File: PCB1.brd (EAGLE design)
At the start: 101.3 x 61 mm, 38 parts

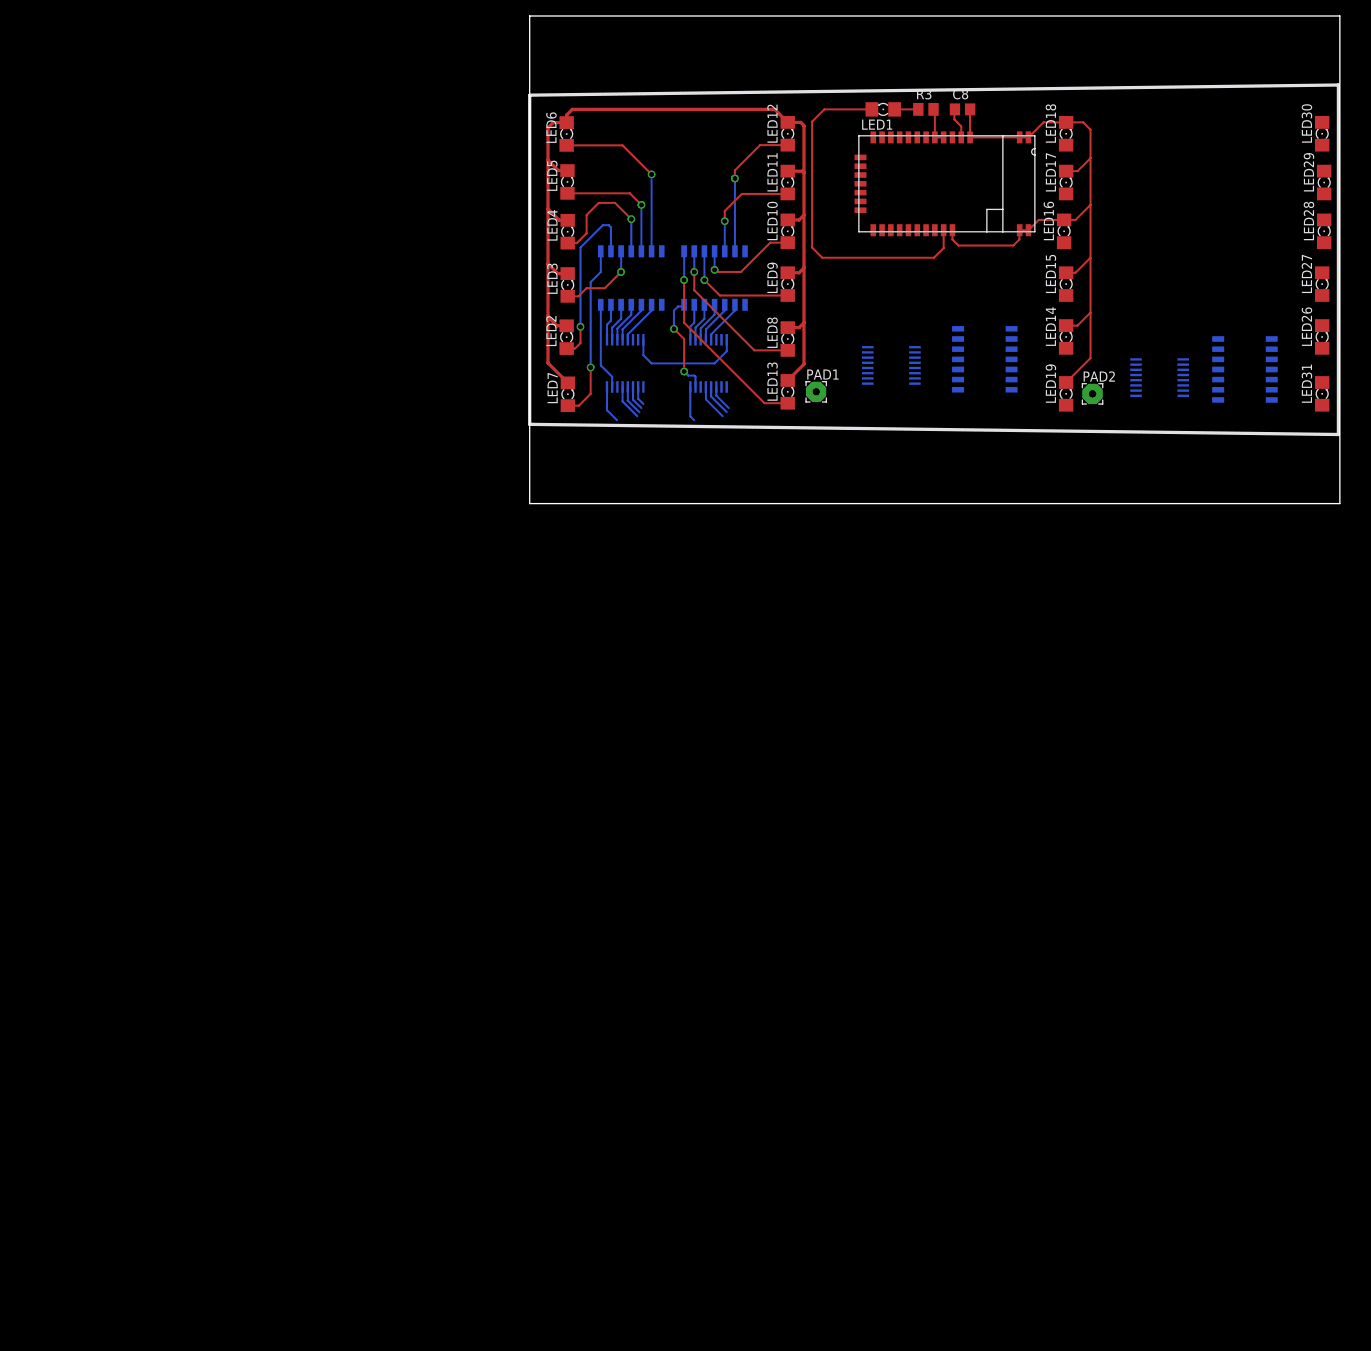
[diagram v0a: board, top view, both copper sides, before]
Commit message: Progress on PCB1 layout. Added solder jumpers to schematic.
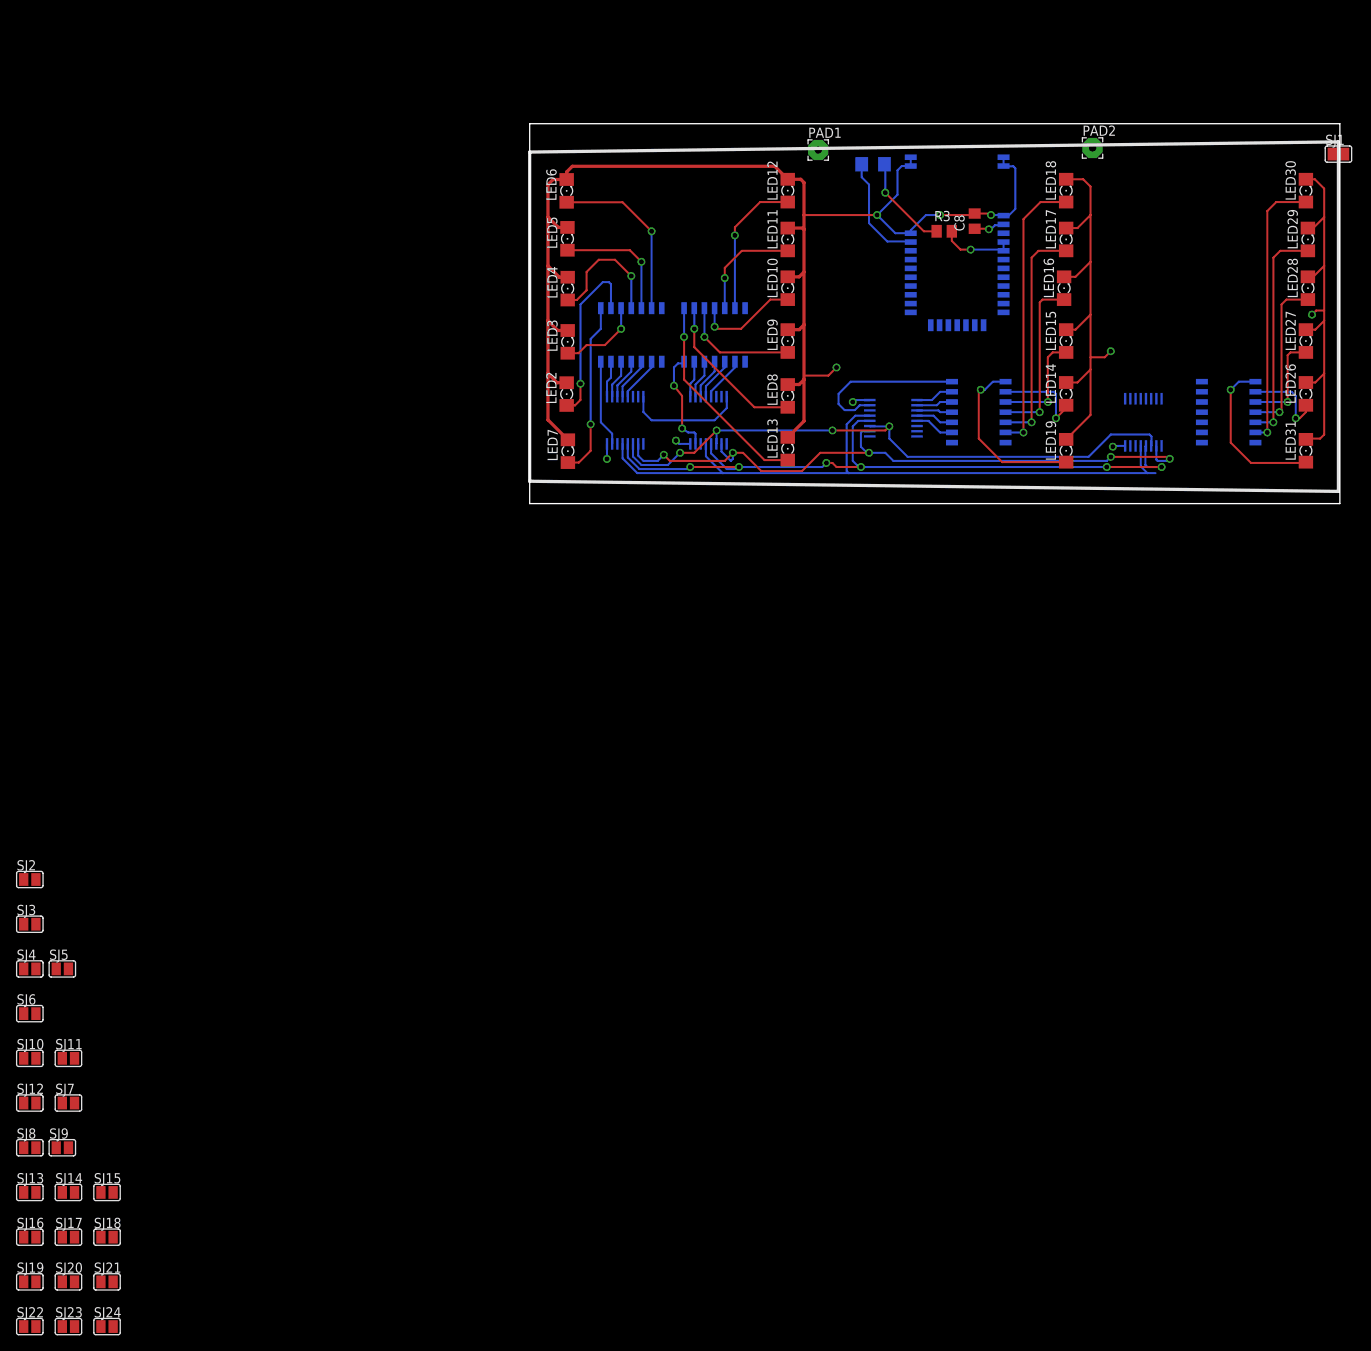
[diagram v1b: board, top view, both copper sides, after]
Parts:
- added SJ1, SJ10, SJ11, SJ12, SJ13, SJ14, SJ15, SJ16, SJ17, SJ18, SJ19, SJ2, SJ20, SJ21, SJ22, SJ23, SJ24, SJ3, SJ4, SJ5, SJ6, SJ7, SJ8, SJ9: (no value), jumper:SJ
- moved PAD2 30.7 mm to (70.4, 44.5)
- moved PAD1 30.2 mm to (36.1, 44.2)
- moved U$2 30.1 mm to (59.4, 22.1), flipped to the bottom, turned to 0 degrees
- moved R3 15.4 mm to (51.8, 34.0)
- moved C8 14.1 mm to (55.6, 35.3), turned to 90 degrees
- moved LED28 7.40 mm to (97.3, 26.9)
- moved LED30 7.40 mm to (97.0, 39.1)
- moved LED26 7.40 mm to (97.0, 13.7)
- moved LED27 7.40 mm to (97.0, 20.3)
- moved LED31 7.40 mm to (97.0, 6.60)
- moved LED29 7.40 mm to (97.3, 33.0)
- moved LED10 7.11 mm to (32.3, 26.9)
- moved LED12 7.11 mm to (32.3, 39.1)
- moved LED16 7.11 mm to (66.8, 26.9)
- moved LED18 7.11 mm to (67.1, 39.1)
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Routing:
- net N$14: track 2.40 -> 83.5 mm, vias 0 -> 5
- net N$51: track 7.71 -> 87.8 mm, vias 0 -> 6
- net G: track 8.94 -> 87.0 mm
- net N$48: track 6.36 -> 77.9 mm, vias 0 -> 4
- net GND: track 220.9 -> 289.5 mm, vias 0 -> 6
- net N$49: track 0.00 -> 35.1 mm, vias 0 -> 1
- net N$72: track 0.00 -> 34.5 mm, vias 0 -> 1
- net LED: track 43.6 -> 13.9 mm
- net N$47: track 0.00 -> 28.5 mm, vias 0 -> 1
- net N$71: track 0.00 -> 27.5 mm, vias 0 -> 1
- net N$41: track 0.00 -> 21.9 mm, vias 0 -> 1
- net N$46: track 0.00 -> 21.2 mm, vias 0 -> 1
- net N$67: track 0.00 -> 20.6 mm, vias 0 -> 1
- net N$40: track 0.00 -> 20.6 mm
- net N$70: track 0.00 -> 20.1 mm, vias 0 -> 1
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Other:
- board size 101.3 x 61 mm -> 101.3 x 47.5 mm

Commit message: Finished PCB1, PCB3, and added parts to ECE477 library
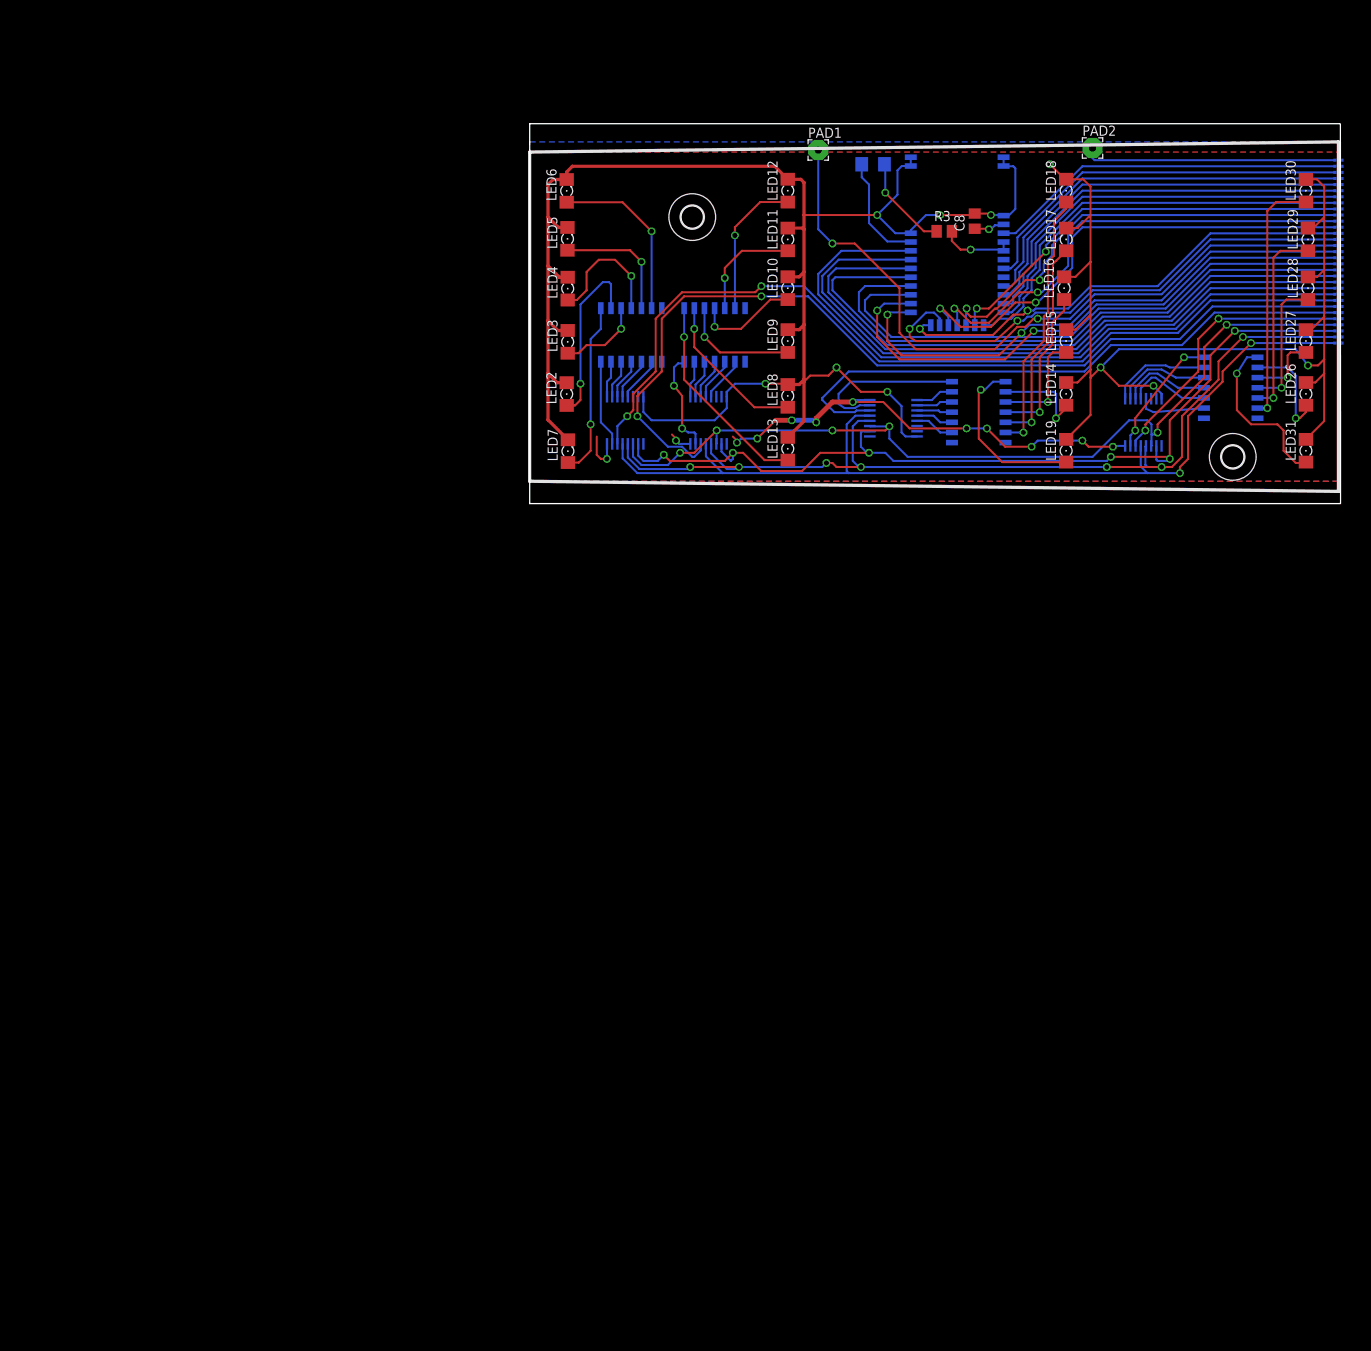
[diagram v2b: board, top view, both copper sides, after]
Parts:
- removed SJ1, SJ10, SJ11, SJ12, SJ13, SJ14, SJ15, SJ16, SJ17, SJ18, SJ19, SJ2, SJ20, SJ21, SJ22, SJ23, SJ24, SJ3, SJ4, SJ5, SJ6, SJ7, SJ8, SJ9: (no value), jumper:SJ
- added H1, H2: MOUNT-HOLE2.8, holes:2,8
- added U$10, U$11, U$12, U$13, U$14, U$15, U$16, U$17, U$18, U$19, U$20, U$21, U$22, U$23, U$24, U$25, U$26, U$27, U$28, U$29, U$30, U$31, U$32, U$33, U$34, U$35, U$36, U$6, U$7, U$8, U$9: JUMPER, ECE477_Guitutar:JUMPER
- moved R5 3.06 mm to (87.6, 14.5)
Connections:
- new net N$100: U$31.P$1
- new net N$101: U$30.P$1
- new net N$102: U$29.P$1
- new net N$103: U$28.P$1
- new net N$104: U$27.P$1
- new net N$105: U$26.P$1
- new net N$106: U$25.P$1
- new net N$107: U$24.P$1
- new net N$108: U$23.P$1
- new net N$109: U$22.P$1
- new net N$110: U$21.P$1
- new net N$111: U$20.P$1
- new net N$112: U$19.P$1
- new net N$113: U$18.P$1
- new net N$114: U$17.P$1
- new net N$115: U$16.P$1
- new net N$13: U$35.P$1
- new net N$17: U$35.P$2
- new net N$18: U$34.P$1
- new net N$31: U$34.P$2
- new net N$32: U$33.P$2
- new net N$33: U$33.P$1
- new net N$34: U$6.P$1
- new net N$42: U$7.P$1
- new net N$45: U$8.P$1
- new net N$50: U$9.P$1
- new net N$52: U$6.P$2
- new net N$53: U$7.P$2
- new net N$54: U$8.P$2
- new net N$55: U$9.P$2
- new net N$56: U$10.P$1
- new net N$57: U$11.P$1
- new net N$58: U$10.P$2
- new net N$59: U$11.P$2
- new net N$65: U$12.P$2
- new net N$73: U$12.P$1
- new net N$74: U$13.P$1
- new net N$75: U$13.P$2
- new net N$76: U$14.P$2
- new net N$77: U$14.P$1
- new net N$78: U$15.P$1
- new net N$79: U$15.P$2
- new net N$80: U$16.P$2
- new net N$81: U$17.P$2
- new net N$82: U$18.P$2
- new net N$83: U$19.P$2
- new net N$84: U$20.P$2
- new net N$85: U$21.P$2
- new net N$86: U$22.P$2
- new net N$87: U$23.P$2
- new net N$88: U$24.P$2
- new net N$89: U$25.P$2
- new net N$90: U$26.P$2
- new net N$91: U$27.P$2
- new net N$92: U$28.P$2
- new net N$93: U$29.P$2
- new net N$94: U$30.P$2
- new net N$95: U$31.P$2
- new net N$96: U$32.P$2
- new net N$97: U$36.P$2
- new net N$98: U$36.P$1
- new net N$99: U$32.P$1
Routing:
- net LED_SER2: track 0.00 -> 116.5 mm, vias 0 -> 2
- net LED_SER1: track 0.00 -> 111.2 mm, vias 0 -> 2
- net FRET1: track 0.00 -> 89.3 mm, vias 0 -> 2
- net P3_7: track 0.00 -> 86.3 mm
- net P3_6: track 0.00 -> 84.5 mm
- net P3_4: track 0.00 -> 82.4 mm
- net P3_3: track 0.00 -> 80.4 mm
- net LED_SER3: track 0.00 -> 75.3 mm
- net P3_2: track 0.00 -> 73.8 mm
- net TXD: track 0.00 -> 71.4 mm, vias 0 -> 2
- net P3_1: track 0.00 -> 71.1 mm
- net RXD: track 0.00 -> 68.3 mm, vias 0 -> 2
- net EAN: track 0.00 -> 65.2 mm, vias 0 -> 2
- net GND: track 289.5 -> 353.0 mm, vias 6 -> 10
- net P2_4: track 0.00 -> 60.1 mm, vias 0 -> 2
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- added copper zone on layer 16, net GND
- added copper zone on layer 1, net VCC
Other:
- board size 101.3 x 47.5 mm -> 101.4 x 47.5 mm
